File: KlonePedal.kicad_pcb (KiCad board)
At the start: 2 copper layers, 58.7 x 91.9 mm, 69 parts, among them J1 Jack-DC, J2 NMJ4HCD2_input, J3 SW1B_DPDT_x2, J4 NMJ4HCD2_output, J5 SW1A_DPDT_x2, U1 TL072, U2 TL072, U3 MAX1044CPA+

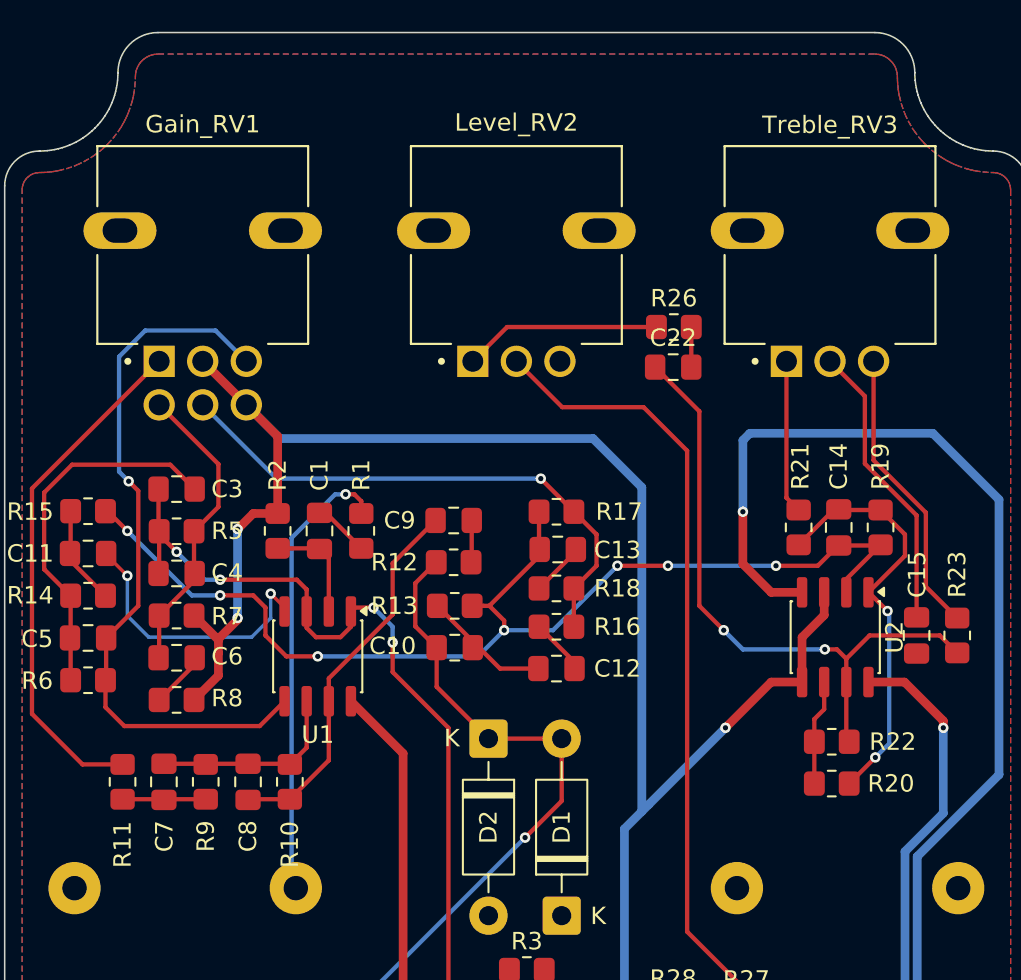
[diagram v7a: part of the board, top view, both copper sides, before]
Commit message: Changed silkscreen font
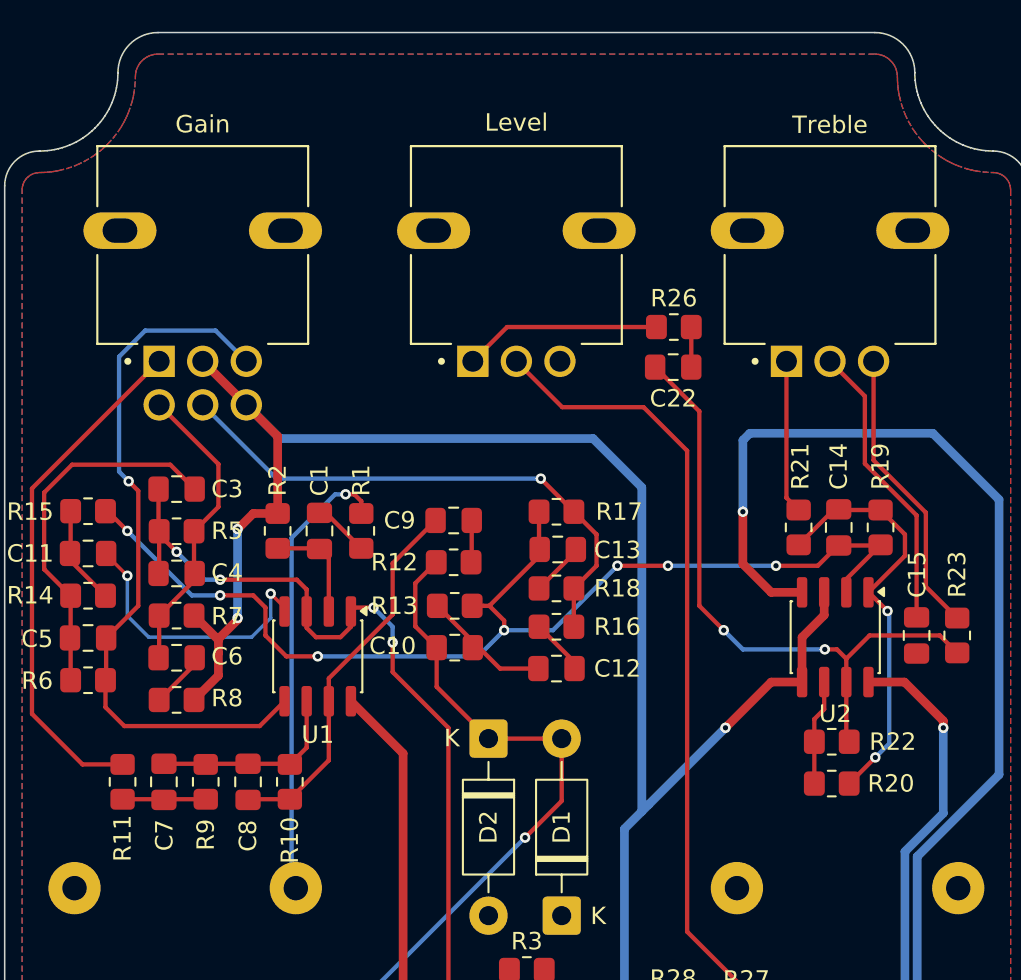
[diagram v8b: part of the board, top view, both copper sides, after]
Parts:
- 9V DC: renamed from J1
- renumbered Gain_RV1 to Gain, J2 to Input, Level_RV2 to Level, J4 to Output, Treble_RV3 to Treble
